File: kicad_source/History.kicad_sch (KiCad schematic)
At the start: 0 parts

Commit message: added page with outputs
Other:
- title: OpenCyphalRobotController07 -> CyphalRobotController07/CAN
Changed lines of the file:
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@@
   (paper "A4")
   (title_block
-    (title "OpenCyphalRobotController07")
-    (date "2023-07-24")
+    (title "CyphalRobotController07/CAN")
+    (date "2023-10-01")
     (rev "0.1")
     (company "generationmake")

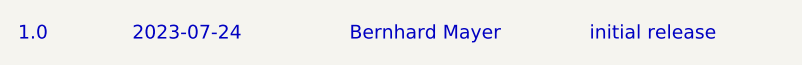
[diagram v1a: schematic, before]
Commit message: added power pole and fuse
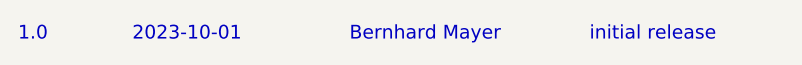
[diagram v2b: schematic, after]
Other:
- note added: "2023-10-01"
- note removed: "2023-07-24"
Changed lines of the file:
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@@
     (company "generationmake")
   )
-  (text "2023-07-24" (at 34.29 22.86 0)
+  (text "2023-10-01" (at 34.29 22.86 0)
     (effects (font (size 1.524 1.524)) (justify left bottom))
   )
